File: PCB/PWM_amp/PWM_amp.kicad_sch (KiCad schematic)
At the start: 38 parts, among them J1 Conn_01x06_Pin, J10 XT30UPB-M, J2 Conn_01x06_Pin, J3 Conn_01x02_Pin, J4 Conn_01x02_Pin, J49 XT60PW-M, J5 XT30UPB-M, Q1 FDD8447L, Q2 FDD8447L, U1 VNH5019A-E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

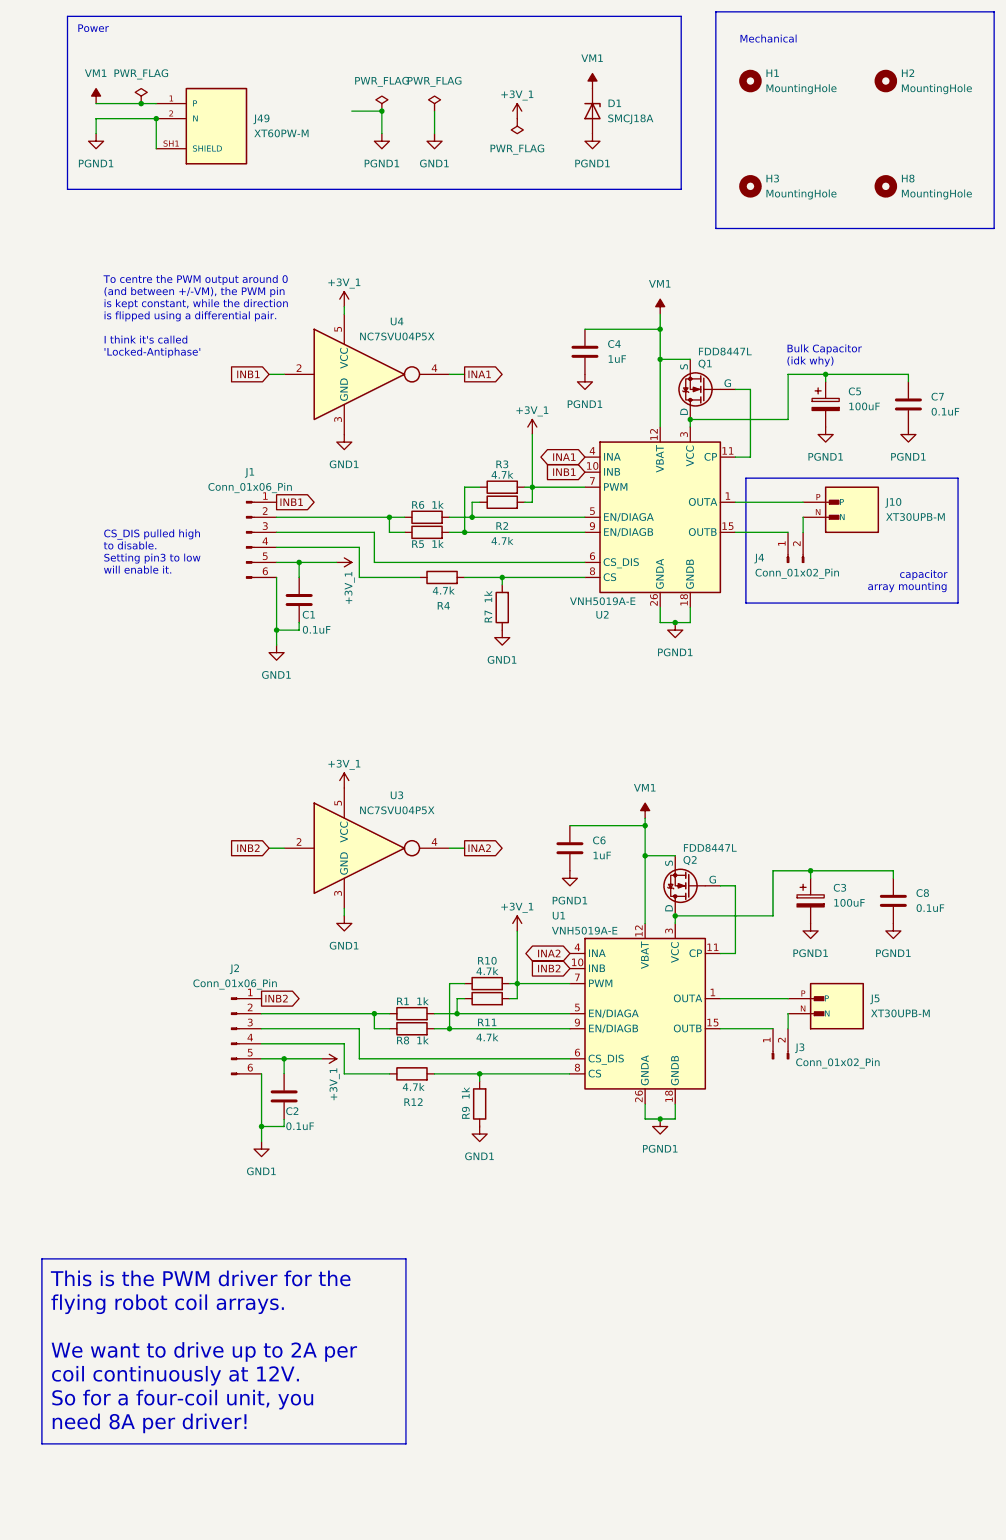
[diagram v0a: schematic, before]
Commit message: fixed up schematic credits
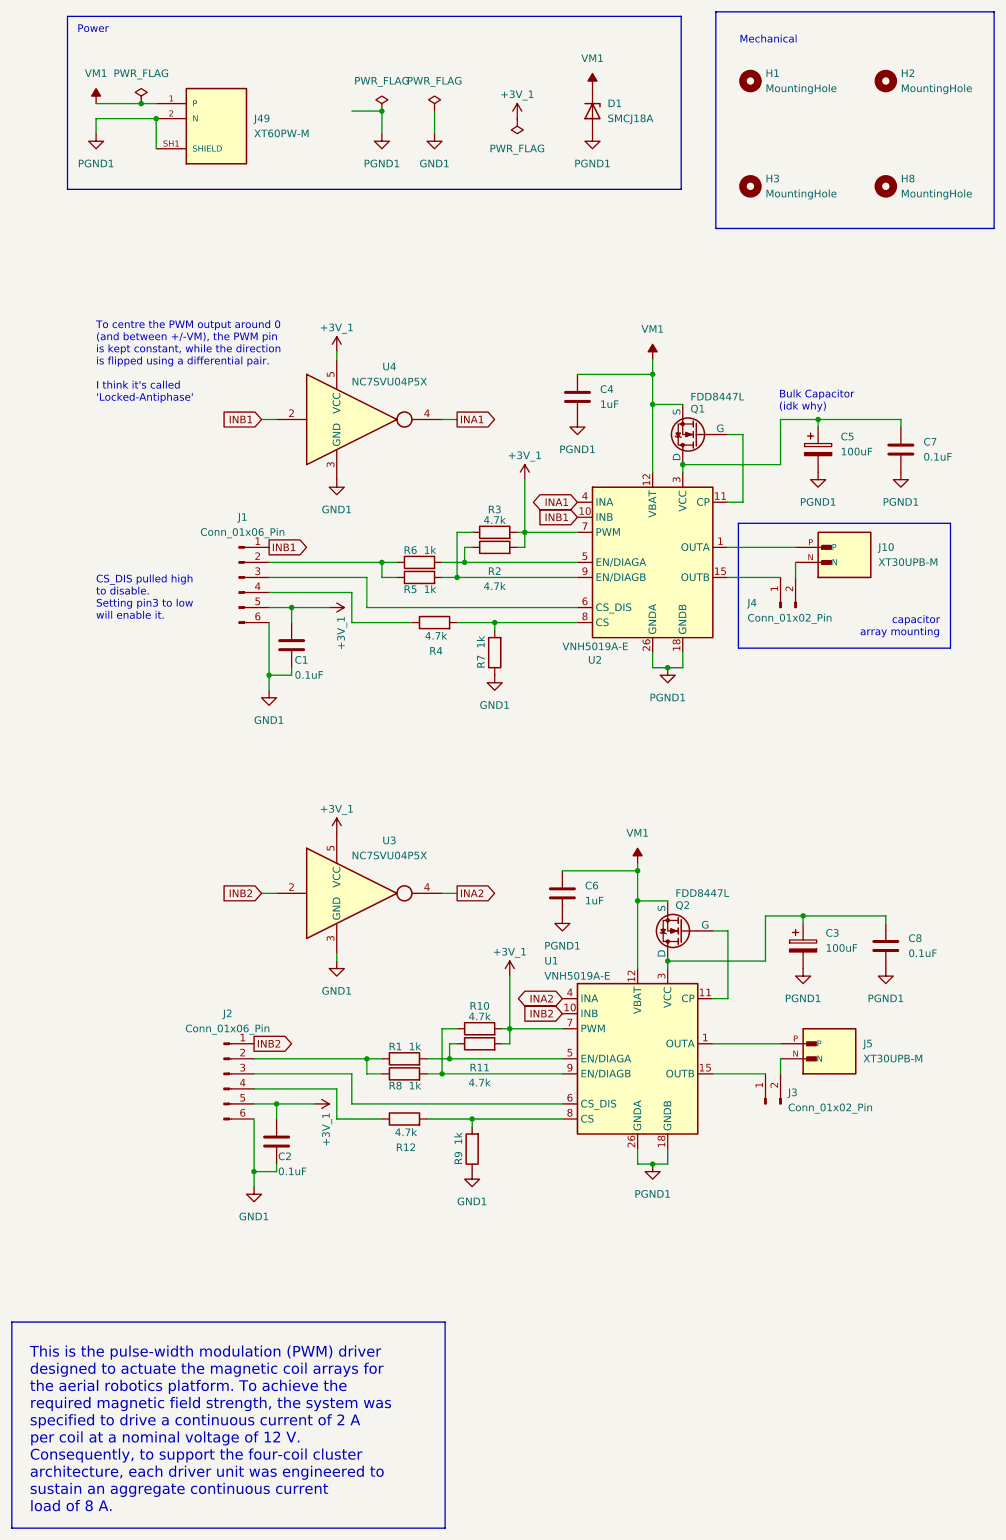
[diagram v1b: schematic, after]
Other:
- note added: "This is the pulse-width modulation (PWM) driver designed to actuate the magnetic coil arrays for the aerial robotics platform. To achieve the required magnetic field strength, the system was specified to drive a continuous current of 2 A per coil at a nominal voltage of 12 V. Consequently, to support the four-coil cluster architecture, each driver unit was engineered to sustain an aggregate conti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"
- note removed: "This is the PWM driver for the flying robot coil arrays. We want to drive up to 2A per coil continuously at 12V. So for a four-coil unit, you need 8A per driver!"
- company: Micro Flying Robots - Liwei Lin Lab -> UC Berkeley, Liwei Lin Lab
- title: PWM Driver -> Two-Channel Magnetic Coil PWM Driver
- moved on the sheet: C1, C2, C3, C4, C5, C6, C7, C8, J1, J10, J2, J3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
